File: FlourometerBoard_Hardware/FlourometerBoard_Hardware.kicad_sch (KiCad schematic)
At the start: 15 parts, among them J1 RJ45_LED_Shielded, J3 Conn_01x09_Pin, U1 Teensy4.1_DEV-16771, U2 OKI, U3 OKI

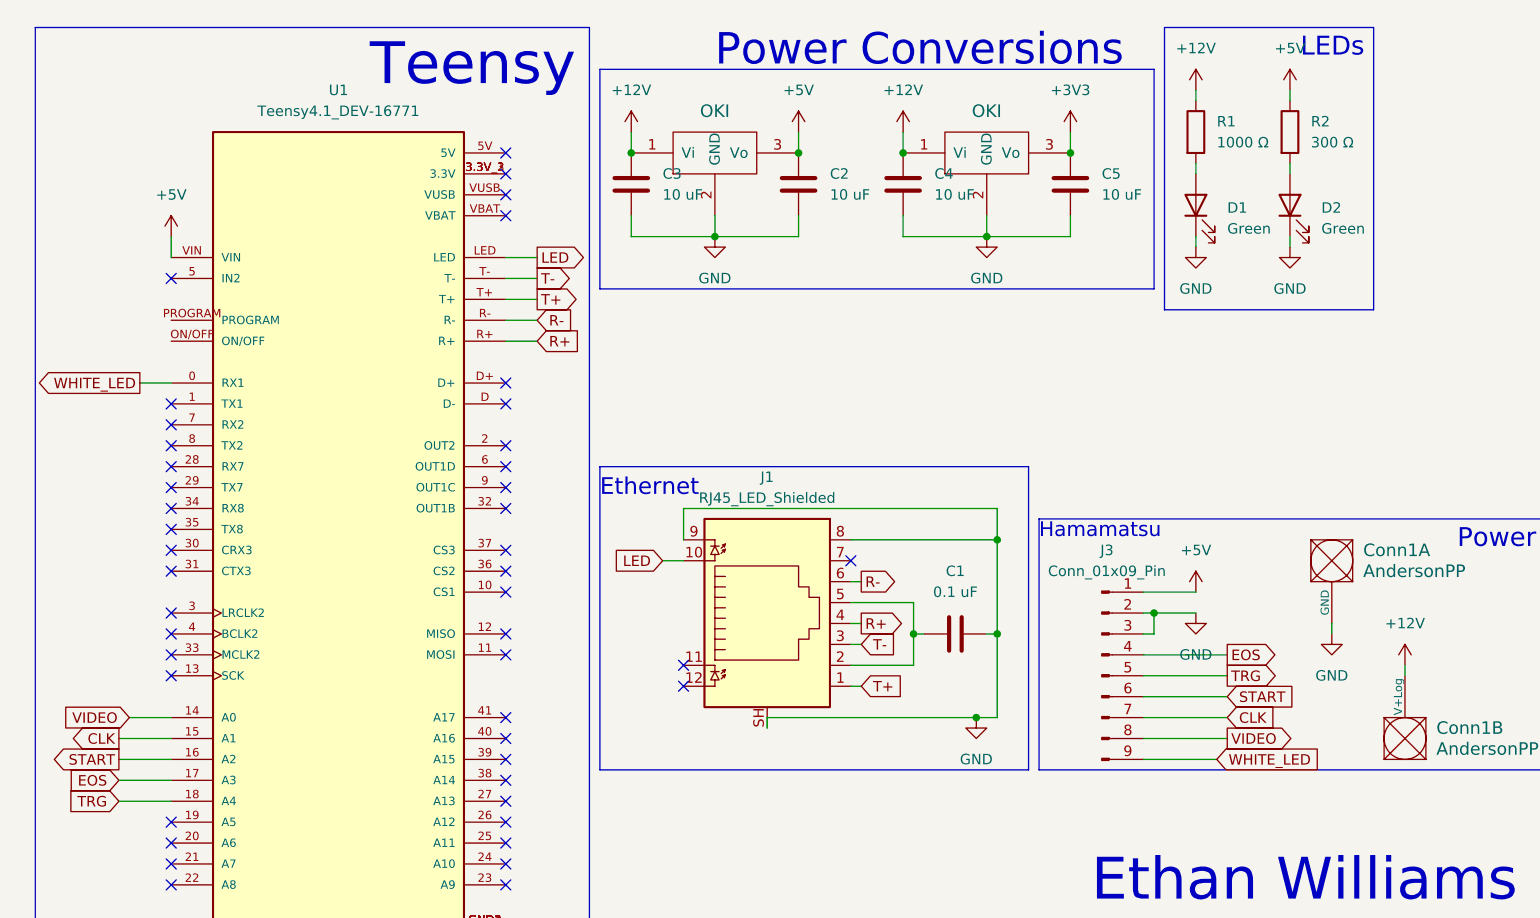
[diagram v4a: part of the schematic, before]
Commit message: Changed Fluoro Connector to Molex, Changed Buck to 3V3
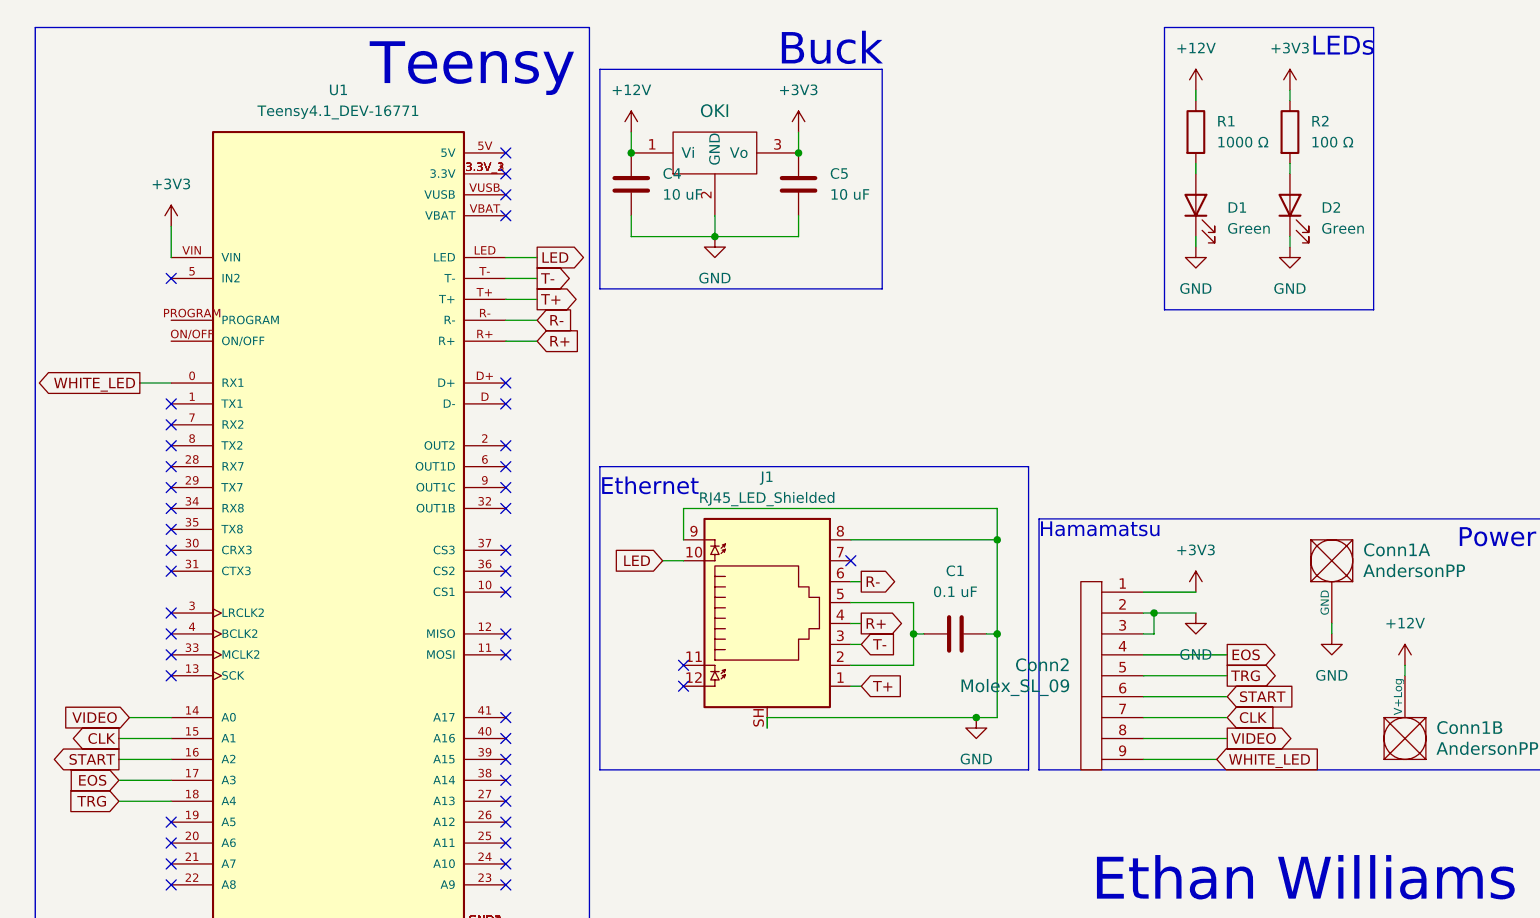
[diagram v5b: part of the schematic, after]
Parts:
- removed C2, C3: 10 uF, Capacitor_SMD:C_0603_1608Metric_Pad1.08x0.95mm_HandSolder, symbol Device:C
- removed J3: Conn_01x09_Pin, MRDT_Connectors:MOLEX_SL_09_Vertical, symbol Connector:Conn_01x09_Pin
- removed U2: OKI, MRDT_Devices:OKI_Horizontal, symbol MRDT_Devices:OKI
- added Conn2: Molex_SL_09, symbol MRDT_Connectors:Molex_SL_09
- R2: value 300 Ω -> 100 Ω
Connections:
- net +5V is gone; now on net +3V3: R2.1, U1.VIN
- net +3V3: now also Conn2.1
- net CLK: now also Conn2.7
- net EOS: now also Conn2.4
- net GND: now also Conn2.2, Conn2.3
- net START: now also Conn2.6
- net TRG: now also Conn2.5
- net VIDEO: now also Conn2.8
- net WHITE_LED: now also Conn2.9
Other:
- note added: "Buck"
- note removed: "Power Conversions"
- moved on the sheet: C4, C5

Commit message: Began Layout, Updated Footprint
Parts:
- Conn1: footprint (none) -> MRDT_Connectors:Square_Anderson_2_H_Side_By_Side_PV
- Conn2: footprint (none) -> MRDT_Connectors:MOLEX_SL_09_Vertical
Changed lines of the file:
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@@
       (effects (font (size 1.524 1.524)) (justify left))
     )
-    (property "Footprint" "" (at 142.24 92.71 0)
+    (property "Footprint" "MRDT_Connectors:MOLEX_SL_09_Vertical" (at 142.24 92.71 0)
       (effects (font (size 1.524 1.524)) hide)
     )
@@
       (effects (font (size 1.524 1.524)) (justify right))
     )
-    (property "Footprint" "" (at 195.58 105.41 0)
-      (effects (font (size 1.524 1.524)) hide)
-    )
+    (property "Footprint" "MRDT_Connectors:Square_Anderson_2_H_Side_By_Side_PV" (at 195.58 105.41 0)
+      (effects (font (size 1.524 1.524)) hide)
+    )

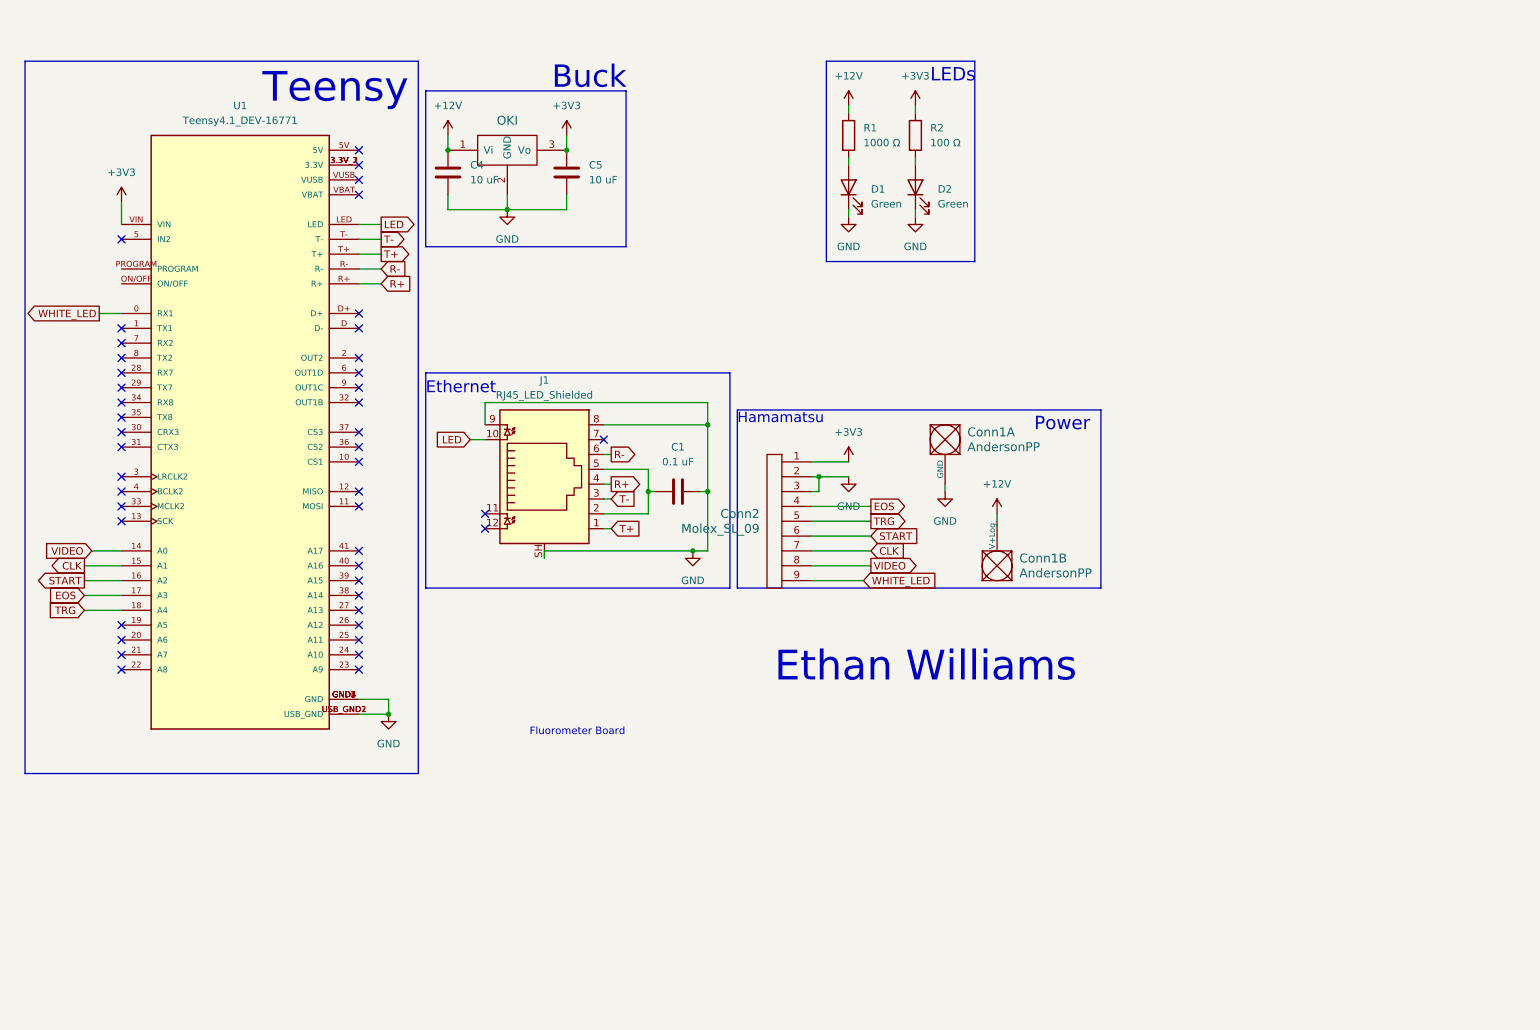
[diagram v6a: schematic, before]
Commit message: Added LED Breakout Connector to Fluoro Board
Also updated footprint for both boards
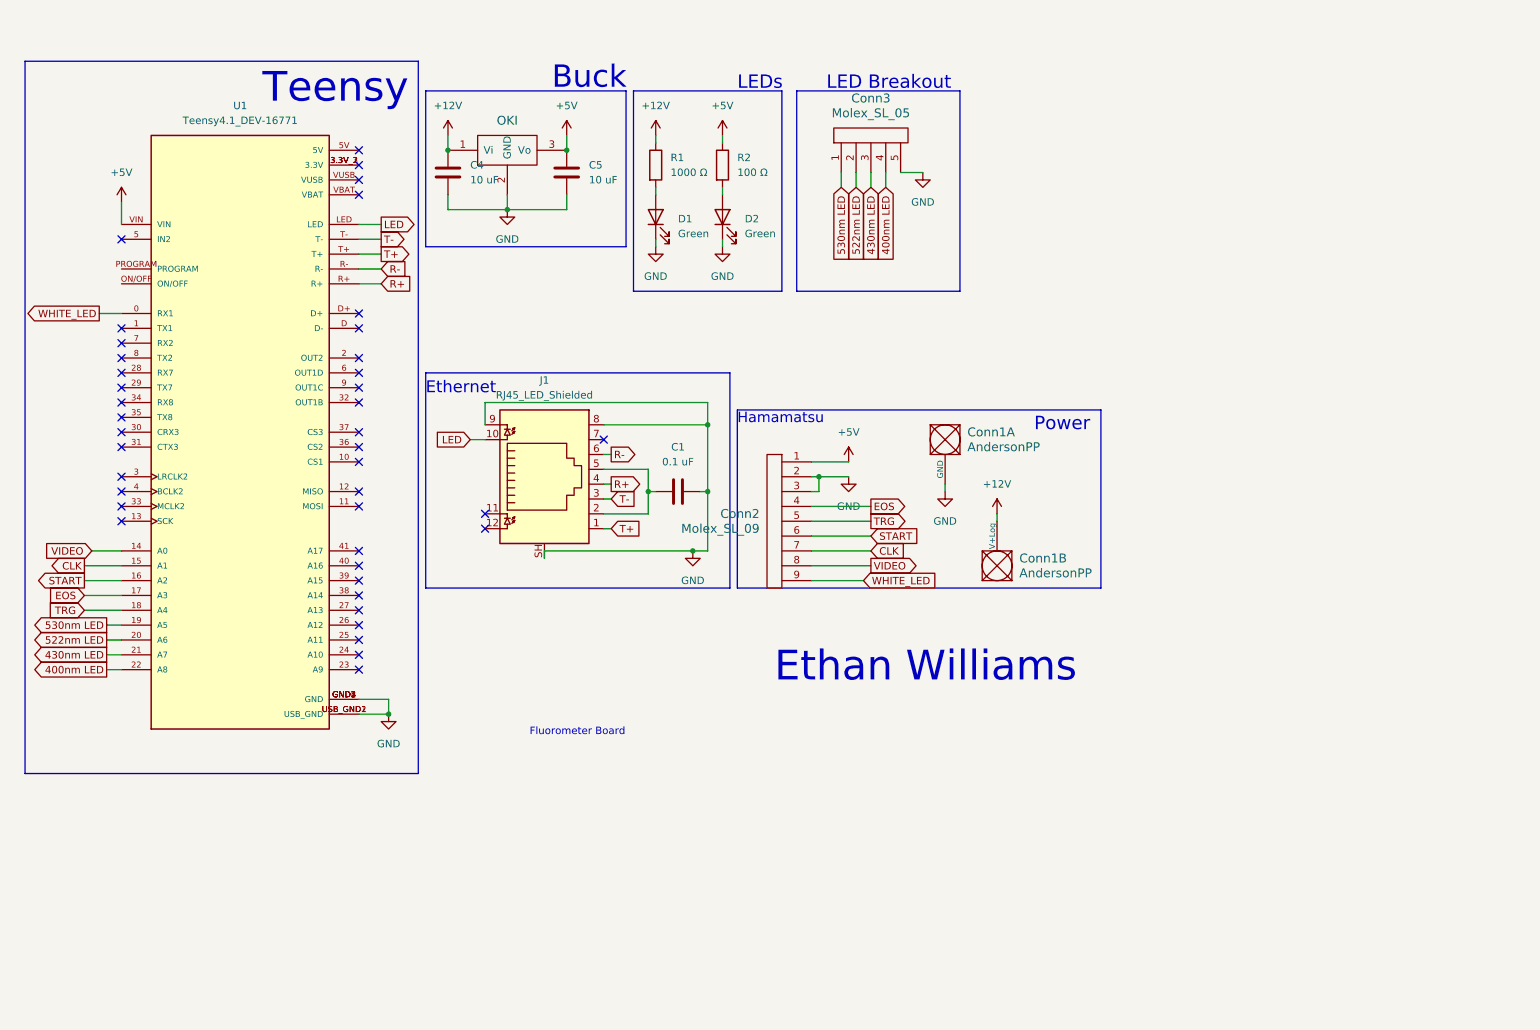
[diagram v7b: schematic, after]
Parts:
- added Conn3: Molex_SL_05, MRDT_Connectors:MOLEX_SL_05_Vertical, symbol MRDT_Connectors:Molex_SL_05
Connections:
- net GND: now also Conn3.5
- net 530nm LED: now reaches U1.19 (A5)
- net 530nm LED: now also Conn3.1
- net 522nm LED: now reaches U1.20 (A6)
- net 522nm LED: now also Conn3.2
- net 430nm LED: now reaches U1.21 (A7)
- net 430nm LED: now also Conn3.3
- net 400nm LED: now reaches U1.22 (A8)
- net 400nm LED: now also Conn3.4
- net +3V3 renamed +5V
- no-connect marks 45 -> 41
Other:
- note added: "LED Breakout"
- moved on the sheet: D1, D2, R1, R2
